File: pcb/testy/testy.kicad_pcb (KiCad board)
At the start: 2 copper layers, 175 x 108 mm, 85 parts, among them U1 ProMicro

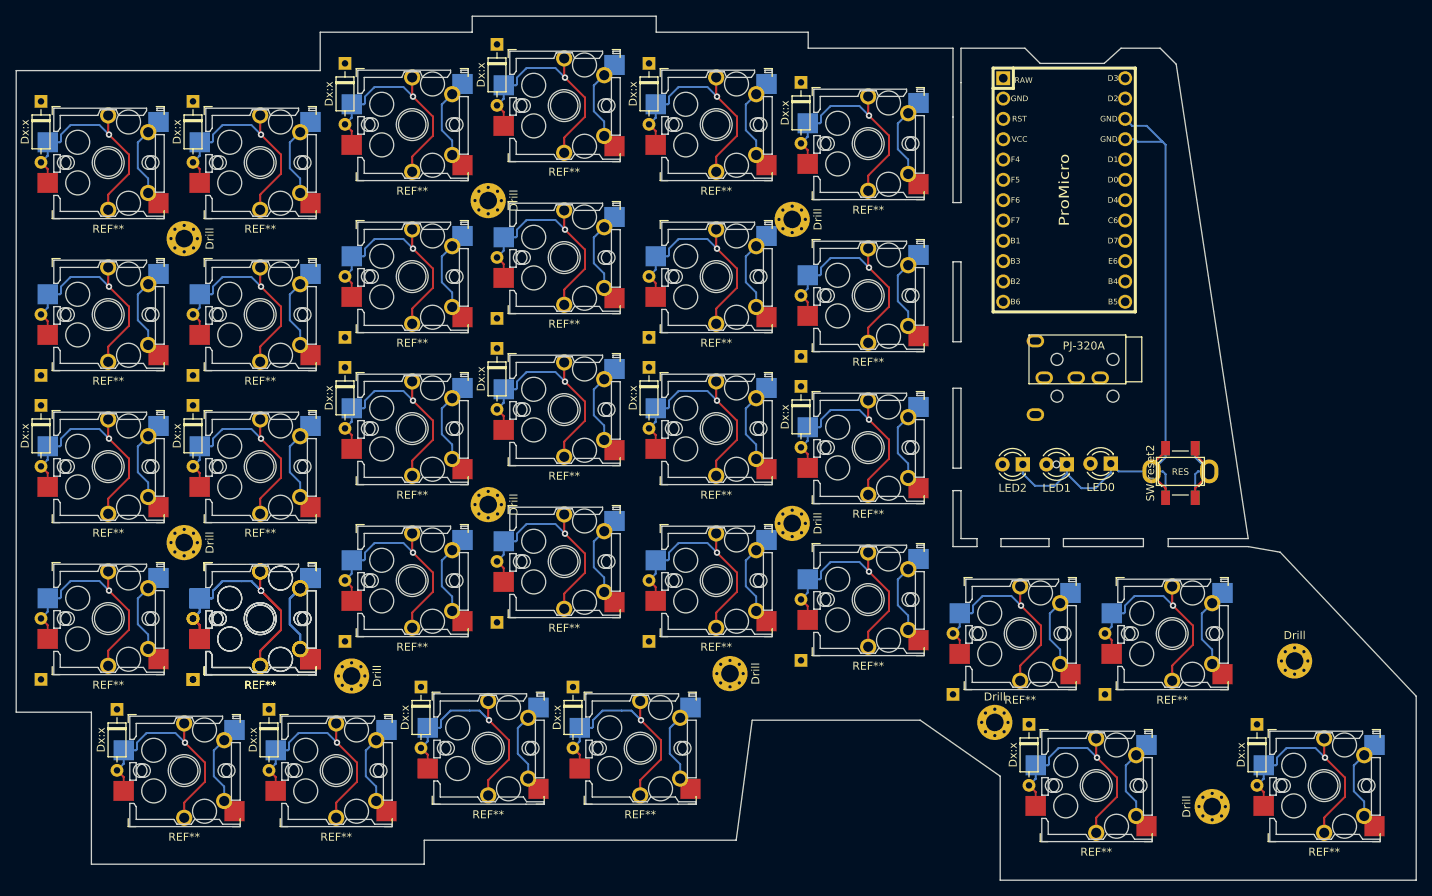
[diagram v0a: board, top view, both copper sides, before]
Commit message: chore: fix misaligned edge cuts, remove some dupe components
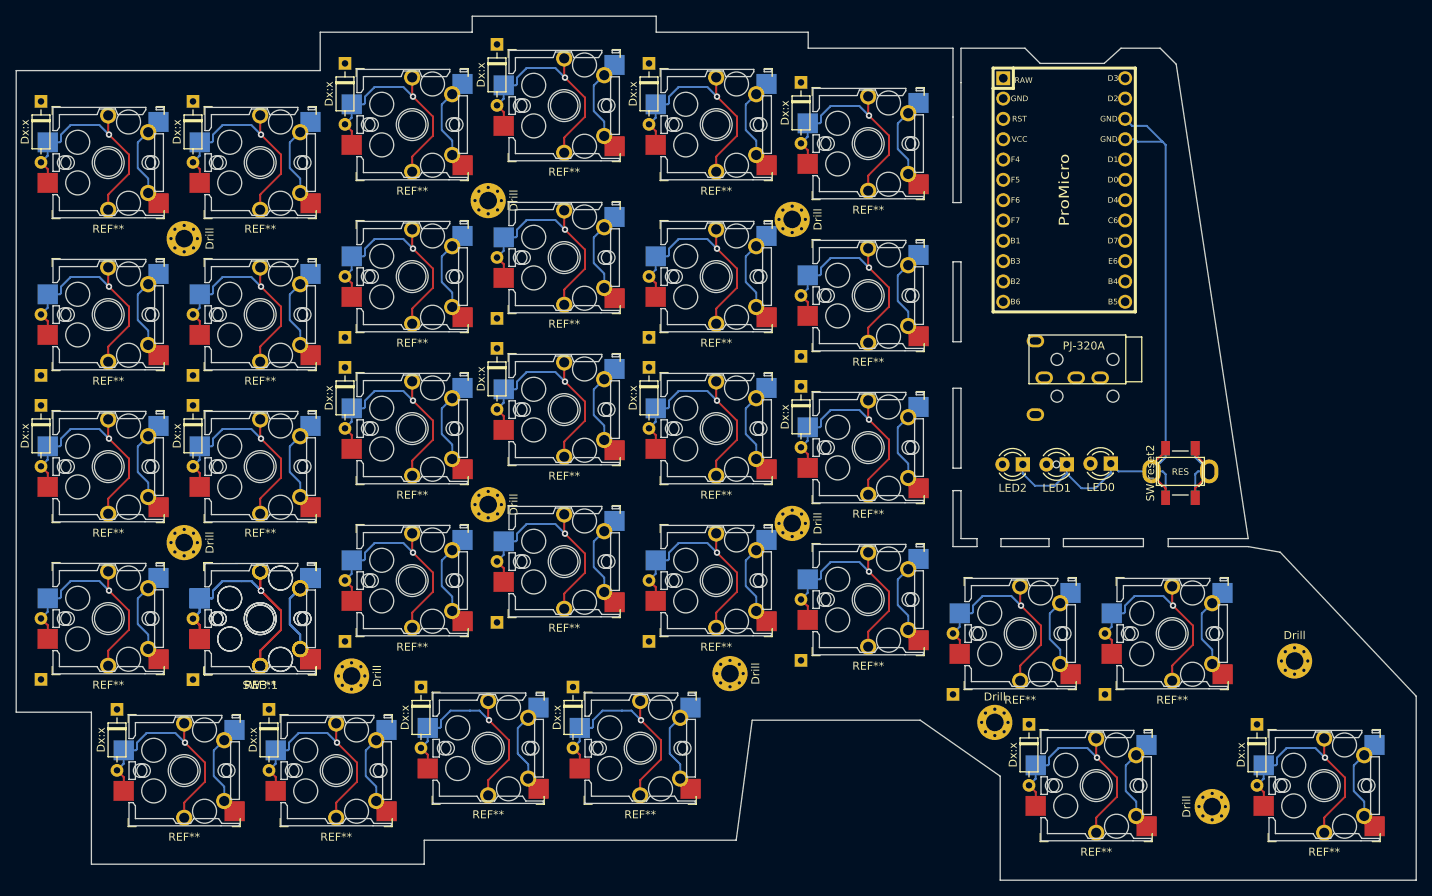
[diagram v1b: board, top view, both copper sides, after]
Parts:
- removed the Dx:x at (92.8, 125.9)
- renumbered REF** to SW3:1
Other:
- outline, holes or cut-outs redrawn

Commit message: feat: some more layout
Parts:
- removed the Drill at (220.2, 141.8)
- removed the Drill at (230.5, 123.6)
- Dx:x: moved to F.Cu
- moved REF** 50.4 mm to (167.8, 137.3)
- moved Drill 50.4 mm to (210.2, 122.0), turned to 0 degrees
- moved Dx:x 47.5 mm to (159.3, 129.6), turned to 270 degrees
- moved Dx:x 47.5 mm to (178.3, 129.6)
- moved REF** 47.5 mm to (186.8, 137.3)
- moved Drill 30.9 mm to (162.7, 125.4)
- moved LED0 19.9 mm to (189.2, 91.1), turned to 270 degrees
- moved TRRS1 13.8 mm to (215.9, 100.4)
- moved SW-reset1 13.5 mm to (211.2, 114.2)
- moved SW-reset2 13.5 mm to (211.2, 112.6)
- moved SW-reset3 13.5 mm to (211.2, 112.6)
- moved LED1 13.0 mm to (189.2, 96.6), turned to 270 degrees
- moved LED2 7.91 mm to (189.2, 102.1), turned to 270 degrees
- moved Dx:x 4.25 mm to (187.8, 123.5)
- moved REF** 4.25 mm to (196.2, 115.9)
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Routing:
- net GND: track 88.0 -> 0.00 mm
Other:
- board size 175 x 108 mm -> 146.6 x 106 mm
- board text added: "TODO add OLED headers"
- board text removed: "<--- Should we have centered holes to make drilling easier?"

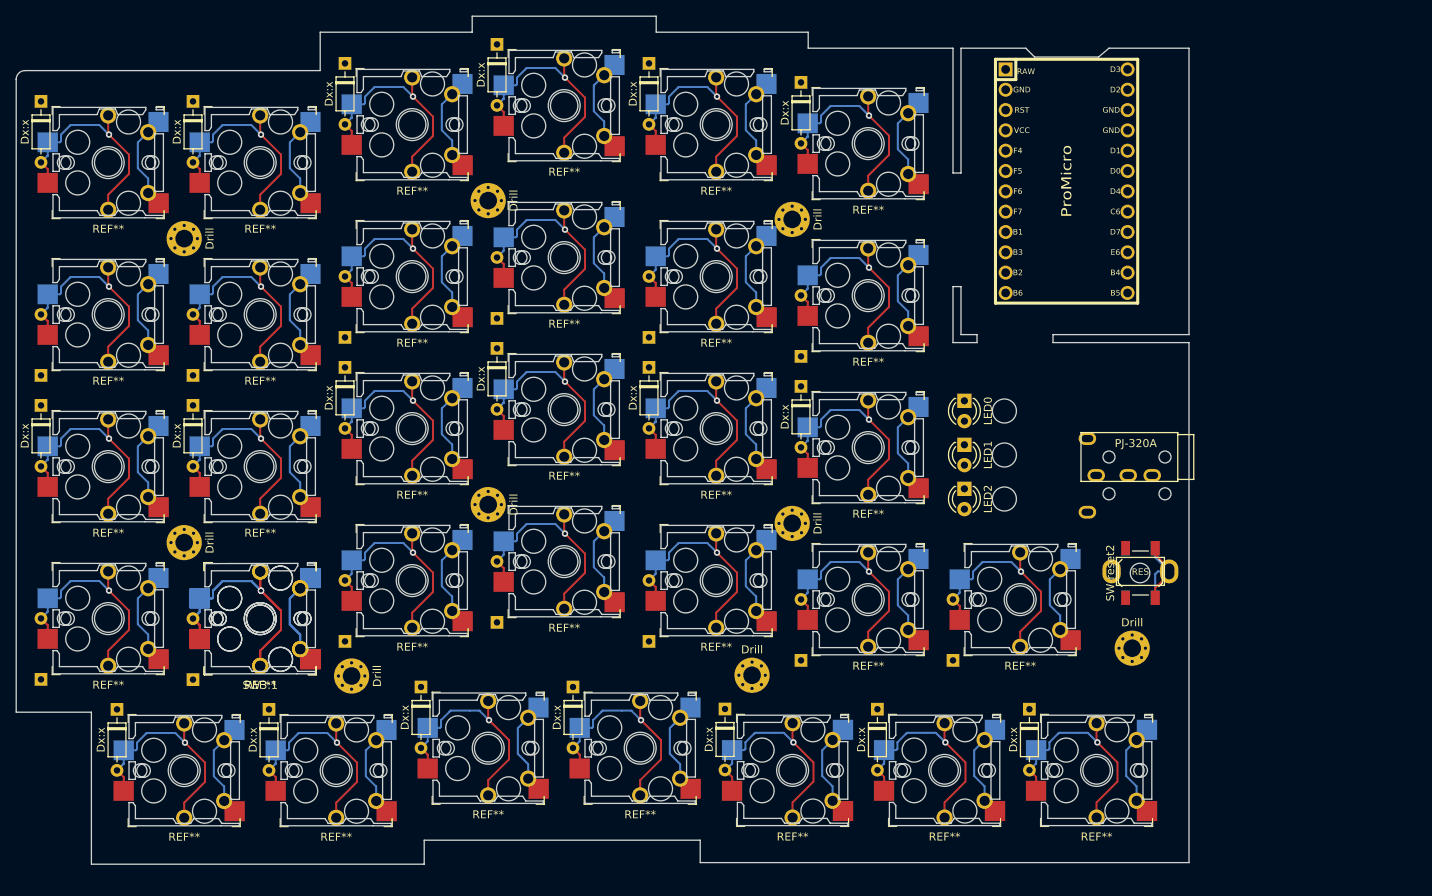
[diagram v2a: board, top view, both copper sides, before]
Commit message: feat: add perforations to pcb
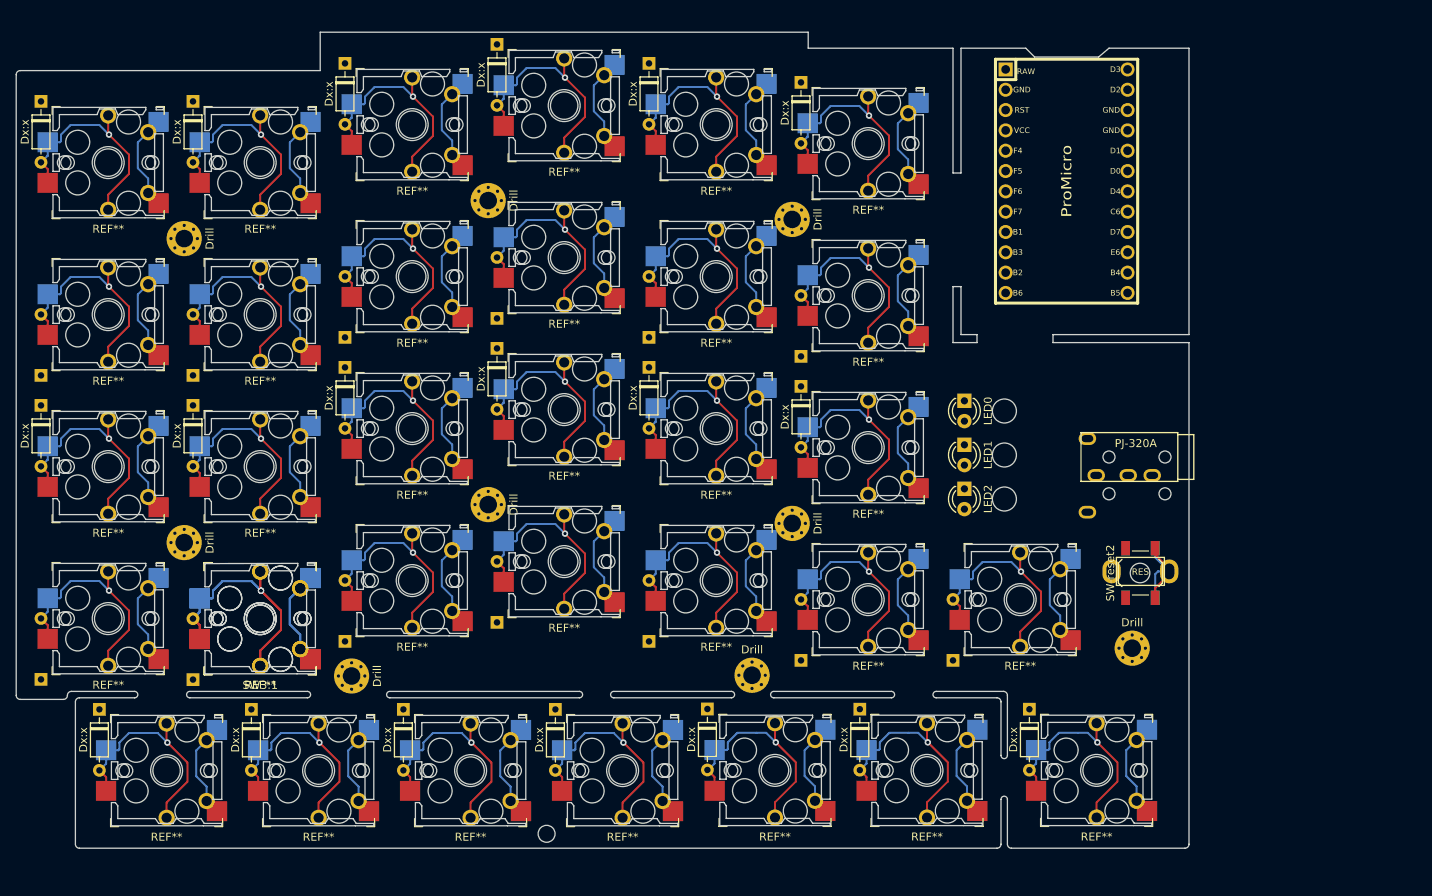
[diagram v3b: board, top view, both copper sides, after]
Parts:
- moved Dx:x 3.56 mm to (138.1, 129.7)
- moved Dx:x 3.56 mm to (119.1, 129.7)
- moved REF** 3.56 mm to (146.5, 137.3)
- moved REF** 3.56 mm to (127.5, 137.3)
- moved Dx:x 2.20 mm to (157.1, 129.6)
- moved Dx:x 2.20 mm to (100.1, 129.7)
- moved Dx:x 2.20 mm to (81.1, 129.7)
- moved REF** 2.20 mm to (108.5, 137.3)
- moved REF** 2.20 mm to (89.5, 137.3)
- moved Dx:x 2.20 mm to (176.2, 129.6)
- moved REF** 2.20 mm to (184.6, 137.3)
- moved REF** 2.20 mm to (165.6, 137.3)
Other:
- board size 146.6 x 106 mm -> 146.6 x 102 mm
- board text added: "\/ Look at moving diodes to inside of board so we can make it a bit narrower"

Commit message: feat: try out moving left edge diodes to inner, tidy up edge cuts of bottom row, add edge connectors for moving thumb switch
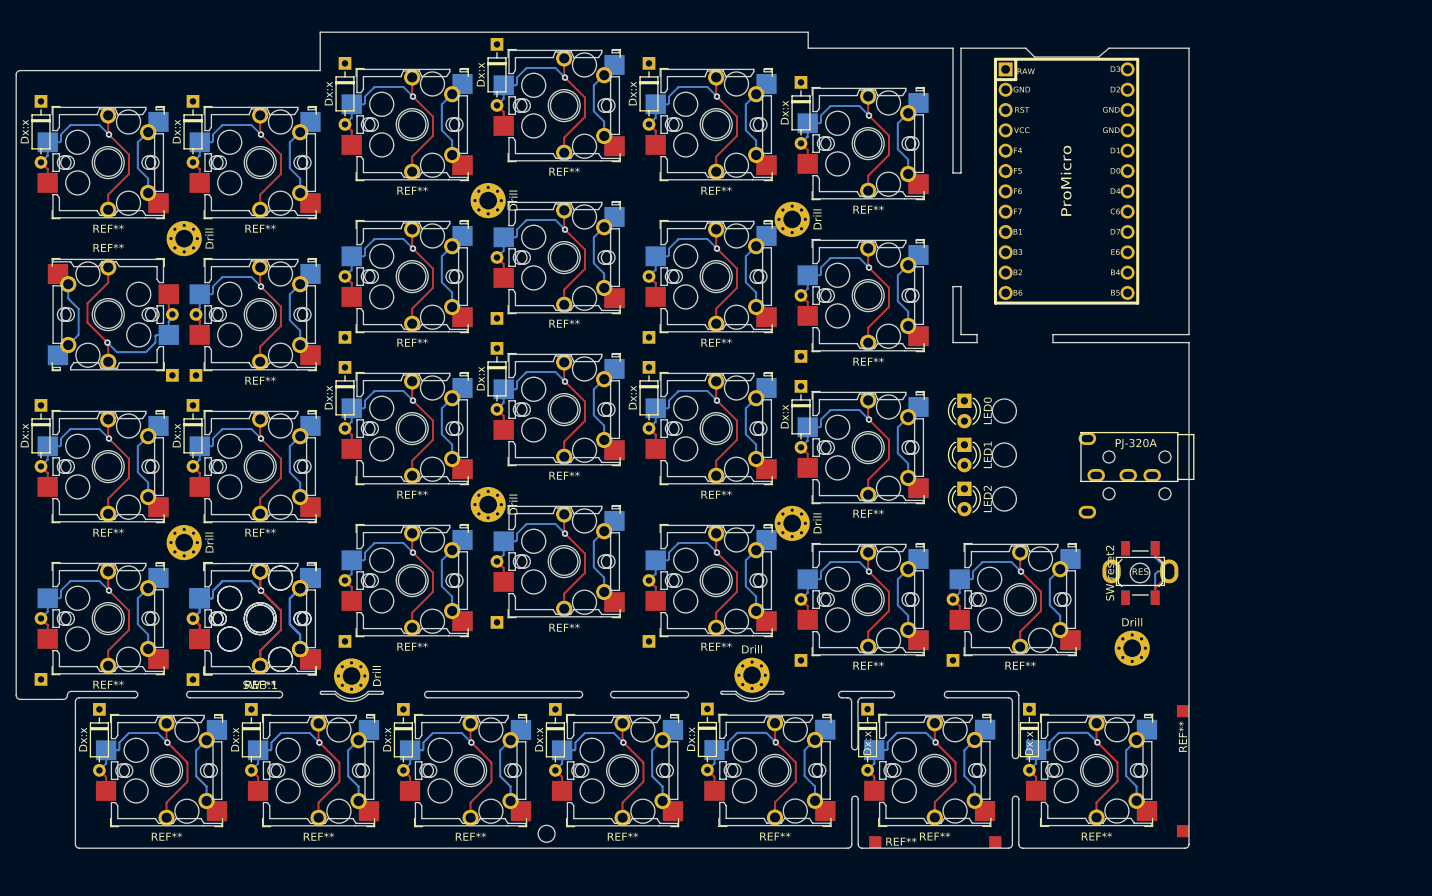
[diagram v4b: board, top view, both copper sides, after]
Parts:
- added REF**: edge-connector, footprints:edge-connector, F.Cu at (216.6, 137.4)
- added REF**: edge-connector, footprints:edge-connector, F.Cu at (185.6, 146.2)
- moved Dx:x 16.4 mm to (90.2, 87.9)
- moved Dx:x 0.97 mm to (177.1, 129.6)
- moved REF** 0.97 mm to (185.5, 137.3)
- moved Dx:x 0.38 mm to (93.2, 87.9)
- turned REF** to 180 degrees
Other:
- outline, holes or cut-outs redrawn
- board text added: "<-- are edge fingers ok, or should we do through holes an mount the extra piece slight higher?"
- board text added: "is there enough clearance between diode and socket pads? -->"

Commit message: flipped left edge diodes, shrunk board a bit
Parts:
- Dx:x (x2): moved to F.Cu
- Dx:x (x2): moved to B.Cu
- moved Dx:x 16.2 mm to (90.0, 53.6)
- moved Dx:x 16.2 mm to (90.0, 125.9)
- moved Dx:x 16.2 mm to (90.0, 91.7)
- moved Dx:x 0.58 mm to (93.4, 125.9)
- moved Dx:x 0.58 mm to (93.4, 91.7)
- moved Dx:x 0.55 mm to (93.3, 53.7)
- turned REF** to 180 degrees (x3)
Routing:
- net (no net): track 1367.8 -> 1454.7 mm
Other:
- board size 146.6 x 102 mm -> 144.9 x 102 mm
- board text added: "<-- add mount for USB-C breakout board Only need mechanical mounting as electrically it'll be a flying lead"
- board text removed: "\/ Look at moving diodes to inside of board so we can make it a bit narrower"
- board text removed: "is there enough clearance between diode and socket pads? -->"
